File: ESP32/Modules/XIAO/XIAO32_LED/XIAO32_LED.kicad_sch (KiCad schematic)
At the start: 0 parts

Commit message: XIAO32_LED: Initial Add of components to sch
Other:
- added sheet Connectors (connectors.kicad_sch)
- added sheet Level Shifter (level_shifter.kicad_sch)
- added sheet MCU (XIAO_ESP32C3.kicad_sch)
- added sheet Mechanical (mechanical.kicad_sch)
- added sheet Power (power.kicad_sch)
- title: (none) -> XIAO32_LED-1

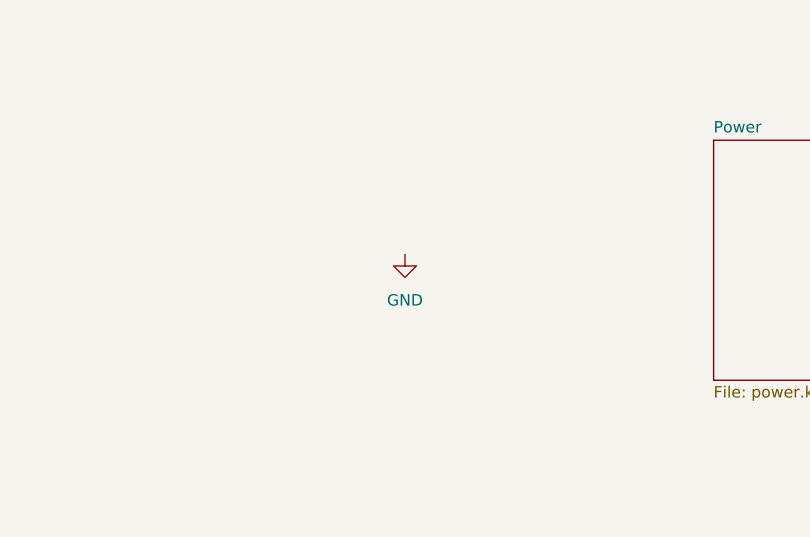
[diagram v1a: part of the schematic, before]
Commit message: XIAO32_LED: MCU wired up
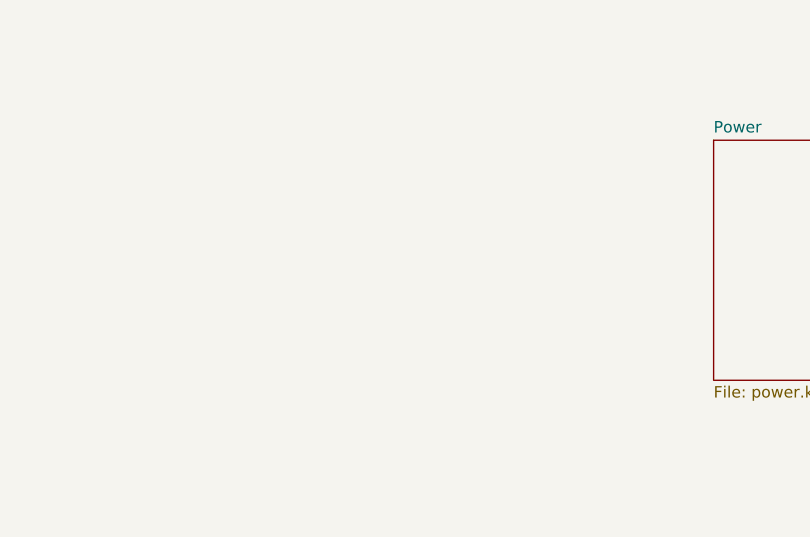
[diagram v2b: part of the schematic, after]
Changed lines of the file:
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@@
 		(rev "A")
-	)
-	(symbol
-		(lib_id "power:GND")
-		(at 166.37 107.95 0)
-		(unit 1)
-		(exclude_from_sim no)
-		(in_bom yes)
-		(on_board yes)
-		(dnp no)
-		(fields_autoplaced yes)
-		(property "Reference" "#PWR01"
-			(at 166.37 114.3 0)
-			(effects
-				(font
-					(size 1.27 1.27)
-				)
-				(hide yes)
-			)
-		)
-		(property "Value" "GND"
-			(at 166.37 113.03 0)
-			(effects
-				(font
-					(size 1.27 1.27)
-				)
-			)
-		)
-		(property "Footprint" ""
-			(at 166.37 107.95 0)
-			(effects
-				(font
-					(size 1.27 1.27)
-				)
-				(hide yes)
-			)
-		)
-		(property "Datasheet" ""
-			(at 166.37 107.95 0)
-			(effects
-				(font
-					(size 1.27 1.27)
-				)
-				(hide yes)
-			)
-		)
-		(property "Description" "Power symbol creates a global label with name \"GND\" , ground"
-			(at 166.37 107.95 0)
-			(effects
-				(font
-					(size 1.27 1.27)
-				)
-				(hide yes)
-			)
-		)
-		(pin "1"
-		)
-		(instances
-			(project ""
-				(path "/68368358-b5ad-4b4d-9ad1-c8762dcf4755"
-					(reference "#PWR01")
-					(unit 1)
-				)
-			)
-		)
 	)
 	(sheet

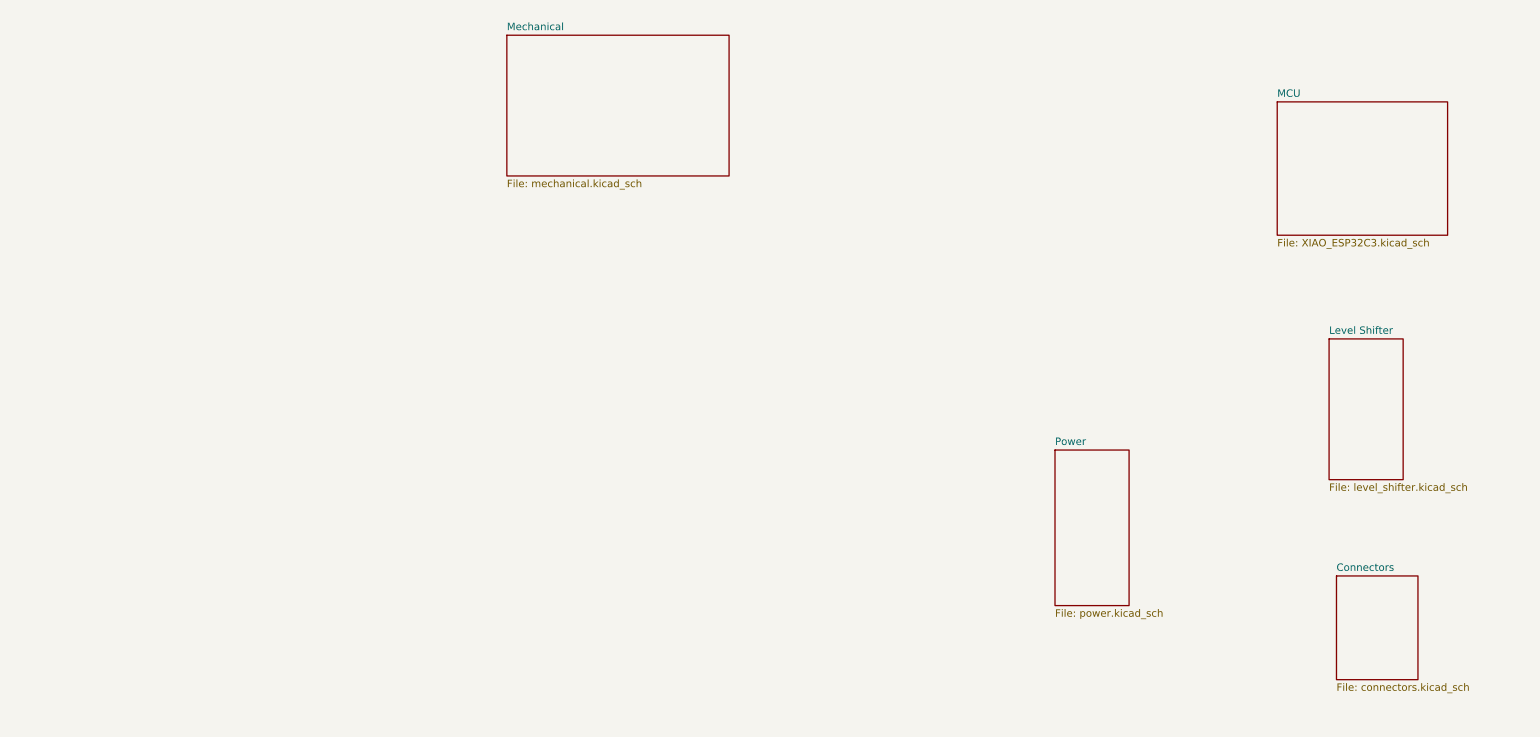
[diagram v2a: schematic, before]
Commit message: XIAO32_LED: Convert sch to hierarchical pins
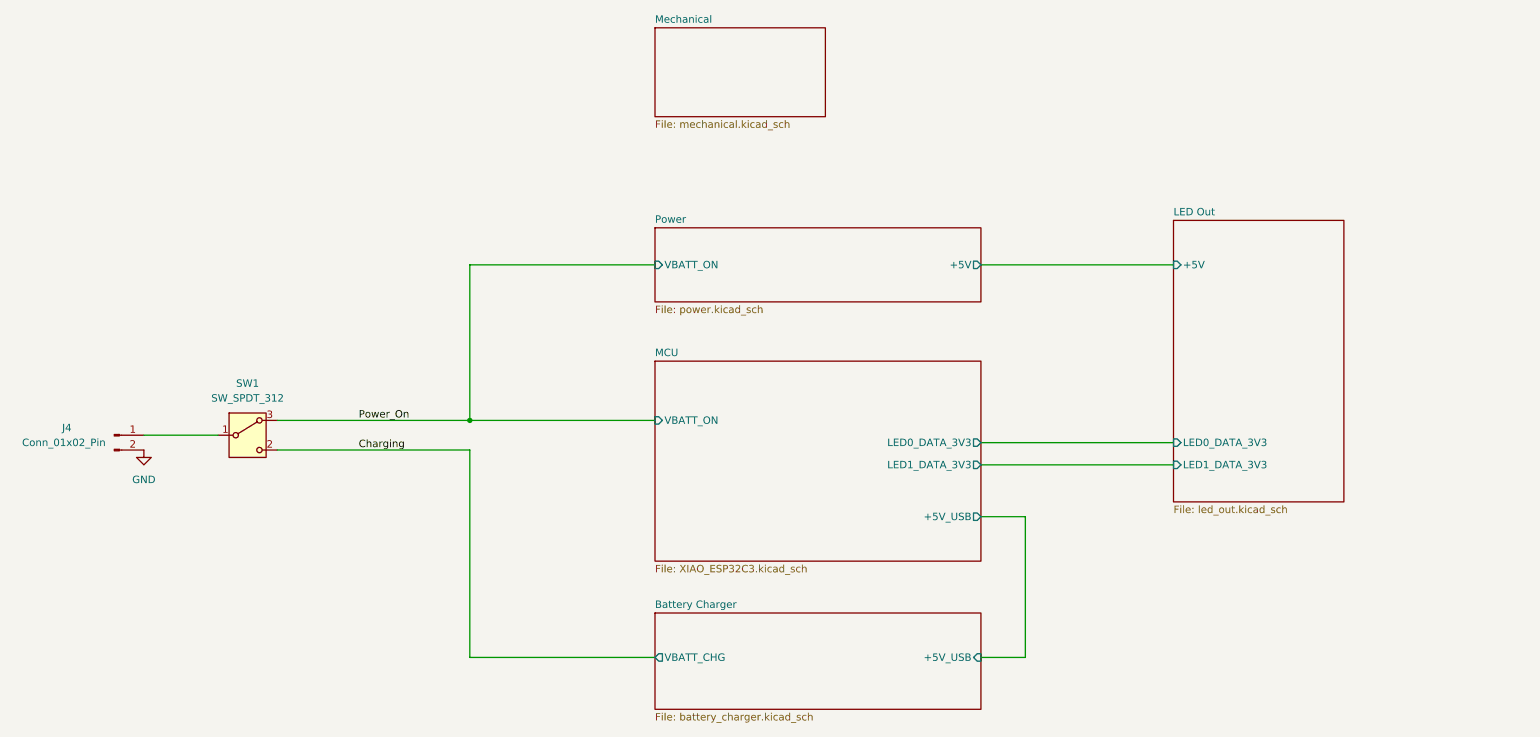
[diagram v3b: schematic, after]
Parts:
- added J4: Conn_01x02_Pin, symbol Connector:Conn_01x02_Pin
- added SW1: SW_SPDT_312, symbol Switch:SW_SPDT_312
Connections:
- new net: J4.1 (Pin_1), SW1.1 (B)
- new net Charging: SW1.2 (C)
- new net GND: J4.2 (Pin_2)
- new net Power_On: SW1.3 (A)
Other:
- removed sheet Connectors
- removed sheet Level Shifter
- added sheet Battery Charger (battery_charger.kicad_sch)
- added sheet LED Out (led_out.kicad_sch)
- sheet MCU ports: added +5V_USB, LED0_DATA_3V3, LED1_DATA_3V3, VBATT_ON; removed none
- sheet Power ports: added +5V, VBATT_ON; removed none
